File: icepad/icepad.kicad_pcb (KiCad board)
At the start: 2 copper layers, 100 x 100 mm, 56 parts, among them J1 Conn_01x04, J2 USB_B_Mini, U1 STM32F042K6Tx, U2 USBLC6-2SC6, U3 TLV62568DRL

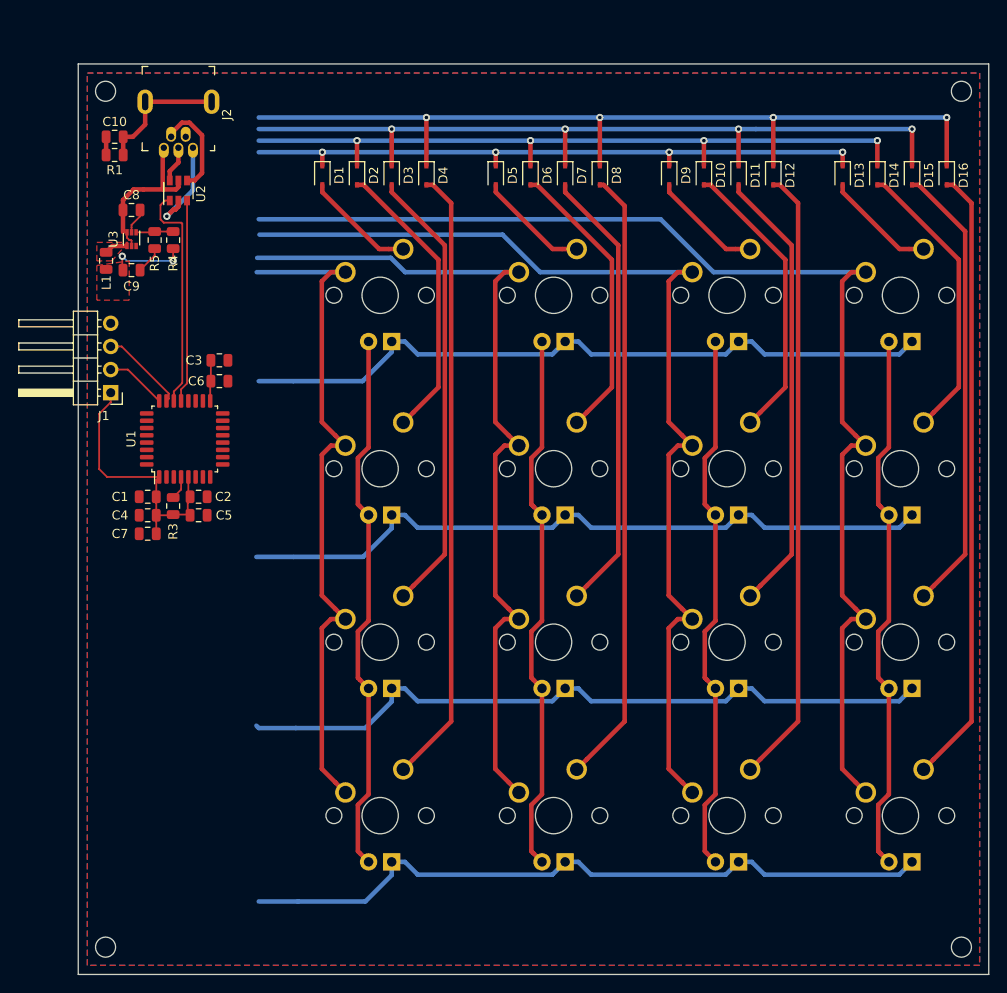
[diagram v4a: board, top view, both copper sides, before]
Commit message: Completed routing, added LED resistors
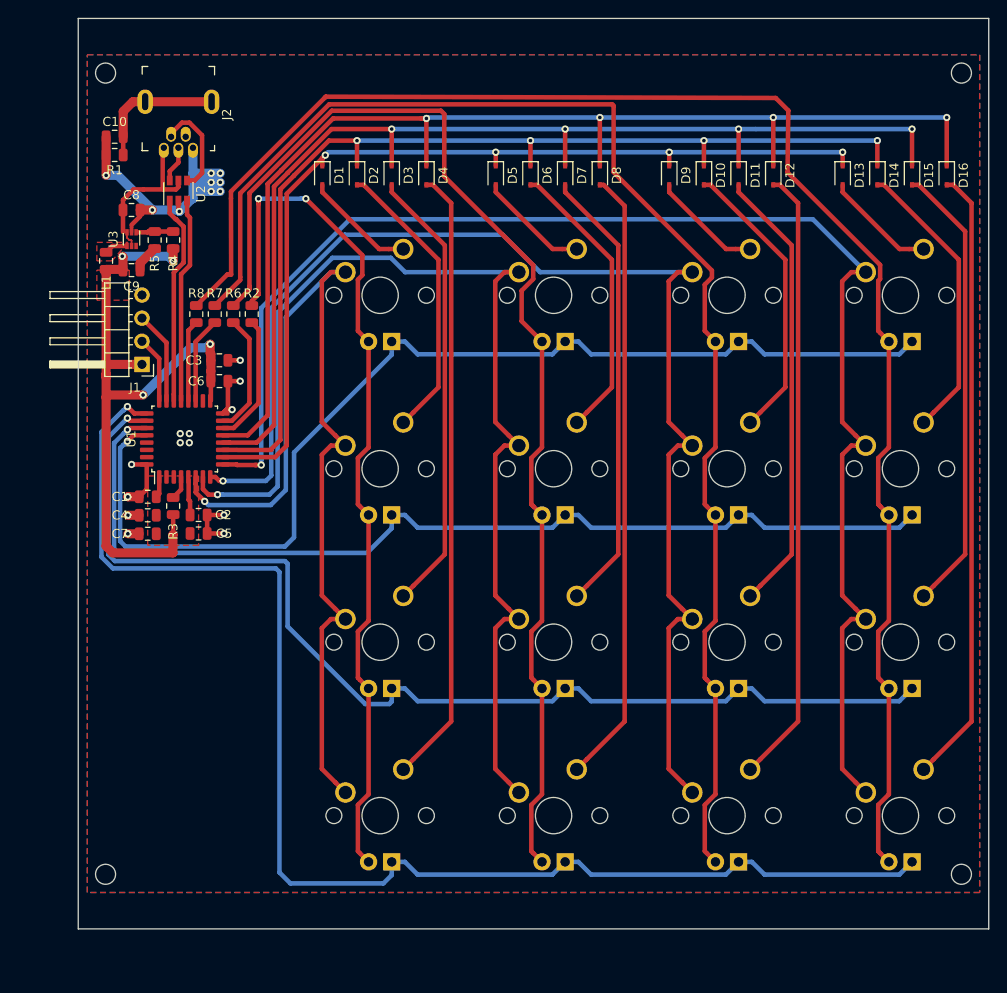
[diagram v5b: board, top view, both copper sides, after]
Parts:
- removed the MNT at (177.0, 147.0)
- removed the MNT at (83.0, 147.0)
- removed the MNT at (177.0, 53.0)
- added MNT: MountingHole_2.2mm_M2, MountingHole:MountingHole_2.2mm_M2, F.Cu at (177.0, 139.0)
- added MNT: MountingHole_2.2mm_M2, MountingHole:MountingHole_2.2mm_M2, F.Cu at (83.0, 139.0)
- added MNT: MountingHole_2.2mm_M2, MountingHole:MountingHole_2.2mm_M2, F.Cu at (177.0, 51.0)
- added R2: 825, Resistor_SMD:R_0805_2012Metric, F.Cu at (99.1, 77.5)
- added R6: 825, Resistor_SMD:R_0805_2012Metric, F.Cu at (97.0, 77.5)
- added R7: 825, Resistor_SMD:R_0805_2012Metric, F.Cu at (95.0, 77.5)
- added R8: 825, Resistor_SMD:R_0805_2012Metric, F.Cu at (93.0, 77.5)
- moved J1 4.63 mm to (87.0, 83.0)
- moved C2 2.00 mm to (93.2, 99.5)
- moved C5 2.00 mm to (93.2, 101.6)
- moved MNT 2.00 mm to (83.0, 51.0)
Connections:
- MX1 pad 3: Col_0_LED -> Net-(MX1-Pad3)
- MX10 pad 3: Col_2_LED -> Net-(MX10-Pad3)
- MX11 pad 3: Col_2_LED -> Net-(MX10-Pad3)
- MX12 pad 3: Col_2_LED -> Net-(MX10-Pad3)
- MX13 pad 3: Col_3_LED -> Net-(MX13-Pad3)
- MX14 pad 3: Col_3_LED -> Net-(MX13-Pad3)
- MX15 pad 3: Col_3_LED -> Net-(MX13-Pad3)
- MX16 pad 3: Col_3_LED -> Net-(MX13-Pad3)
- MX2 pad 3: Col_0_LED -> Net-(MX1-Pad3)
- MX3 pad 3: Col_0_LED -> Net-(MX1-Pad3)
- MX4 pad 3: Col_0_LED -> Net-(MX1-Pad3)
- MX5 pad 3: Col_1_LED -> Net-(MX5-Pad3)
- MX6 pad 3: Col_1_LED -> Net-(MX5-Pad3)
- MX7 pad 3: Col_1_LED -> Net-(MX5-Pad3)
- MX8 pad 3: Col_1_LED -> Net-(MX5-Pad3)
- MX9 pad 3: Col_2_LED -> Net-(MX10-Pad3)
- U1 pad 10: (no net) -> Row_0_Key
- U1 pad 11: (no net) -> Row_1_Key
- U1 pad 12: (no net) -> Row_2_Key
- U1 pad 13: (no net) -> Row_3_Key
- U1 pad 14: (no net) -> Col_0_LED
- U1 pad 15: (no net) -> Col_1_LED
- U1 pad 19: (no net) -> Col_2_LED
- U1 pad 20: (no net) -> Col_3_LED
- U1 pad 25: (no net) -> Row_3_LED
- U1 pad 26: (no net) -> Row_2_LED
- U1 pad 27: (no net) -> Row_1_LED
- U1 pad 28: (no net) -> Row_0_LED
- U1 pad 6: (no net) -> Col_0_Key
- U1 pad 7: (no net) -> Col_1_Key
- U1 pad 8: (no net) -> Col_2_Key
- U1 pad 9: (no net) -> Col_3_Key
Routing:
- net Net-(MX13-Pad3): track 0.00 -> 170.9 mm
- net Net-(MX10-Pad3): track 0.00 -> 149.9 mm
- net Net-(MX5-Pad3): track 0.00 -> 128.9 mm
- net Net-(MX1-Pad3): track 0.00 -> 97.1 mm, vias 0 -> 2
- net Row_3_LED: track 77.9 -> 148.7 mm, vias 0 -> 1
- net GND: track 19.5 -> 80.4 mm, vias 1 -> 22
- net +3V3: track 43.4 -> 95.2 mm, vias 2 -> 4
- net Col_3_LED: track 60.1 -> 8.96 mm
- net Col_2_LED: track 60.1 -> 9.47 mm
- net Col_1_LED: track 60.1 -> 13.3 mm
- net Col_0_LED: track 60.1 -> 14.2 mm
- net Row_2_LED: track 78.3 -> 122.2 mm, vias 0 -> 1
- net Row_0_LED: track 77.7 -> 120.1 mm, vias 0 -> 1
- net Row_1_Key: track 79.0 -> 113.0 mm
- net Row_0_Key: track 70.1 -> 103.9 mm
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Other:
- net class Default: clearance 0.2 -> 0.13
- net class Key Matrix: clearance 0.2 -> 0.13
- net class POWER added: clearance 0.13, trace_width 1, via_dia 0.8, via_drill 0.4
- rule trace_clearance: 0.2 -> 0.13

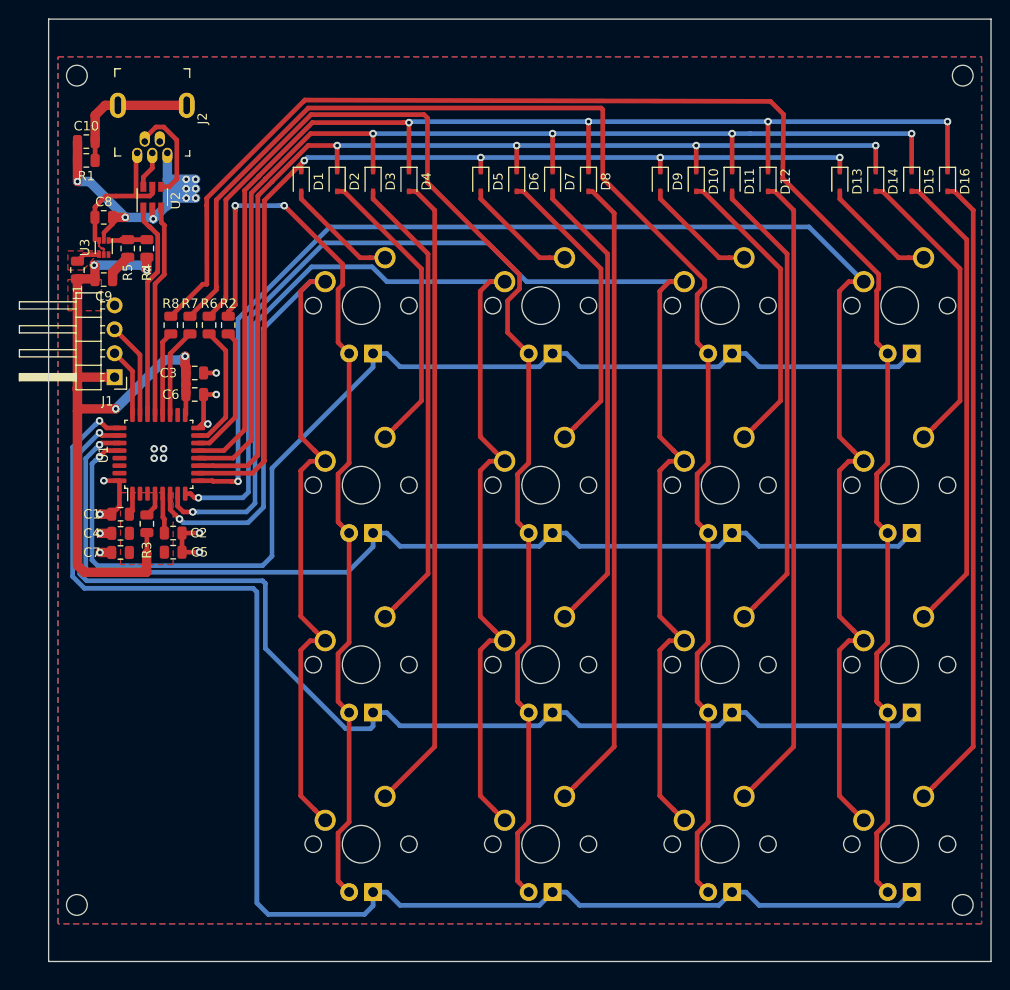
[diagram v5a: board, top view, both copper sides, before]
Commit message: added potentiometers and 3d models
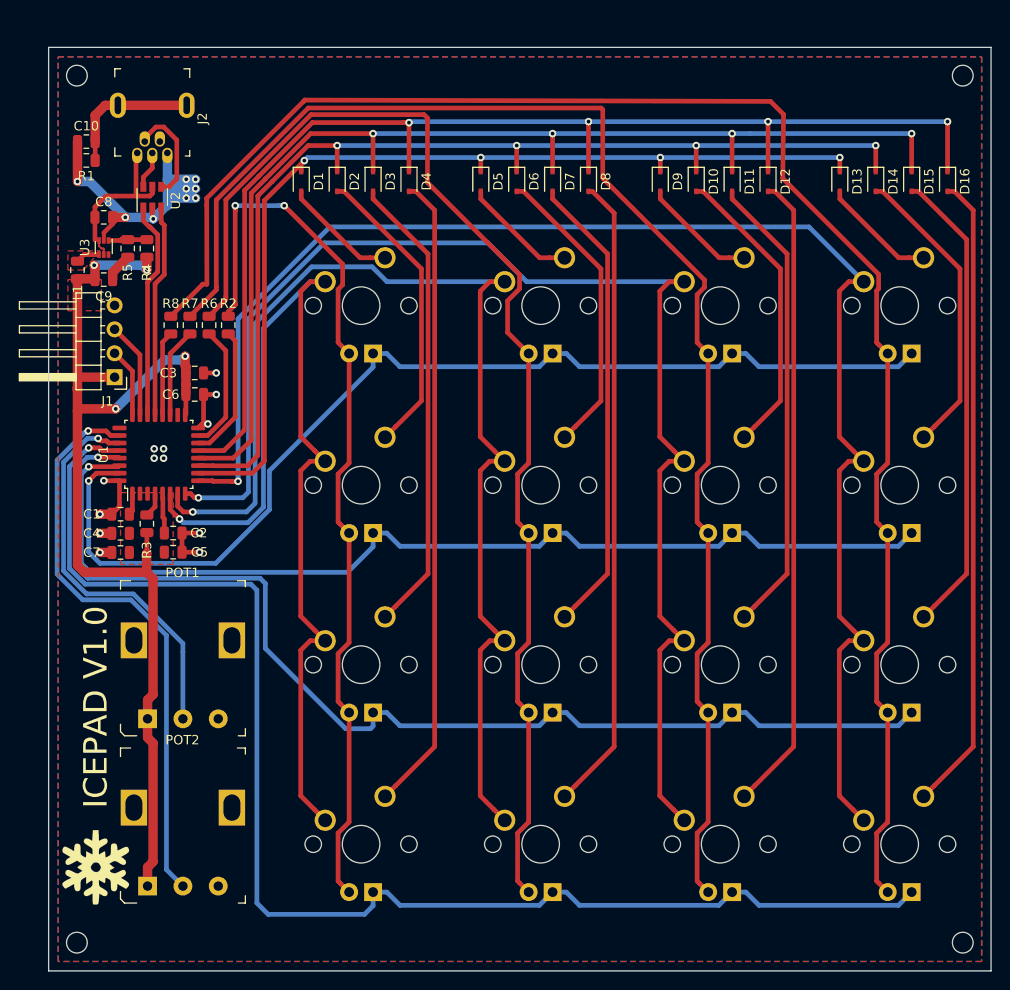
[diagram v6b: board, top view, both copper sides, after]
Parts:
- removed the MNT at (177.0, 139.0)
- removed the MNT at (83.0, 139.0)
- added G***: LOGO, logo:logo, F.Cu at (85.0, 135.0)
- added MNT: MountingHole_2.2mm_M2, MountingHole:MountingHole_2.2mm_M2, F.Cu at (177.0, 143.0)
- added MNT: MountingHole_2.2mm_M2, MountingHole:MountingHole_2.2mm_M2, F.Cu at (83.0, 143.0)
- added POT1: P120PK-Y25BR10K, pot:Potentiometer_P120PK-Y25BR10K, F.Cu at (90.5, 119.2)
- added POT2: P120PK-Y25BR10K, pot:Potentiometer_P120PK-Y25BR10K, F.Cu at (90.5, 137.0)
- J2: footprint digikey-footprints:USB_Mini_B_Female_548190519 -> usb:USB_Mini_B_Female_548190519
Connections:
- U1 pad 25: Row_3_LED -> (no net)
- U1 pad 26: Row_2_LED -> POT2
- U1 pad 27: Row_1_LED -> POT1
- U1 pad 28: Row_0_LED -> Row_3_LED
- U1 pad 29: (no net) -> Row_2_LED
- U1 pad 30: (no net) -> Row_1_LED
- U1 pad 31: (no net) -> Row_0_LED
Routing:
- net POT2: track 0.00 -> 61.8 mm, vias 0 -> 1
- net POT1: track 0.00 -> 42.6 mm, vias 0 -> 1
- net +3V3: track 95.2 -> 129.5 mm
- net Row_0_LED: track 120.1 -> 115.0 mm
- net Row_3_LED: track 148.7 -> 146.3 mm
- net Row_2_LED: track 122.2 -> 120.5 mm
- net Row_1_LED: track 109.8 -> 108.5 mm
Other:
- board size 100 x 100 mm -> 100 x 98 mm
- board text added: "ICEPAD V1.0"

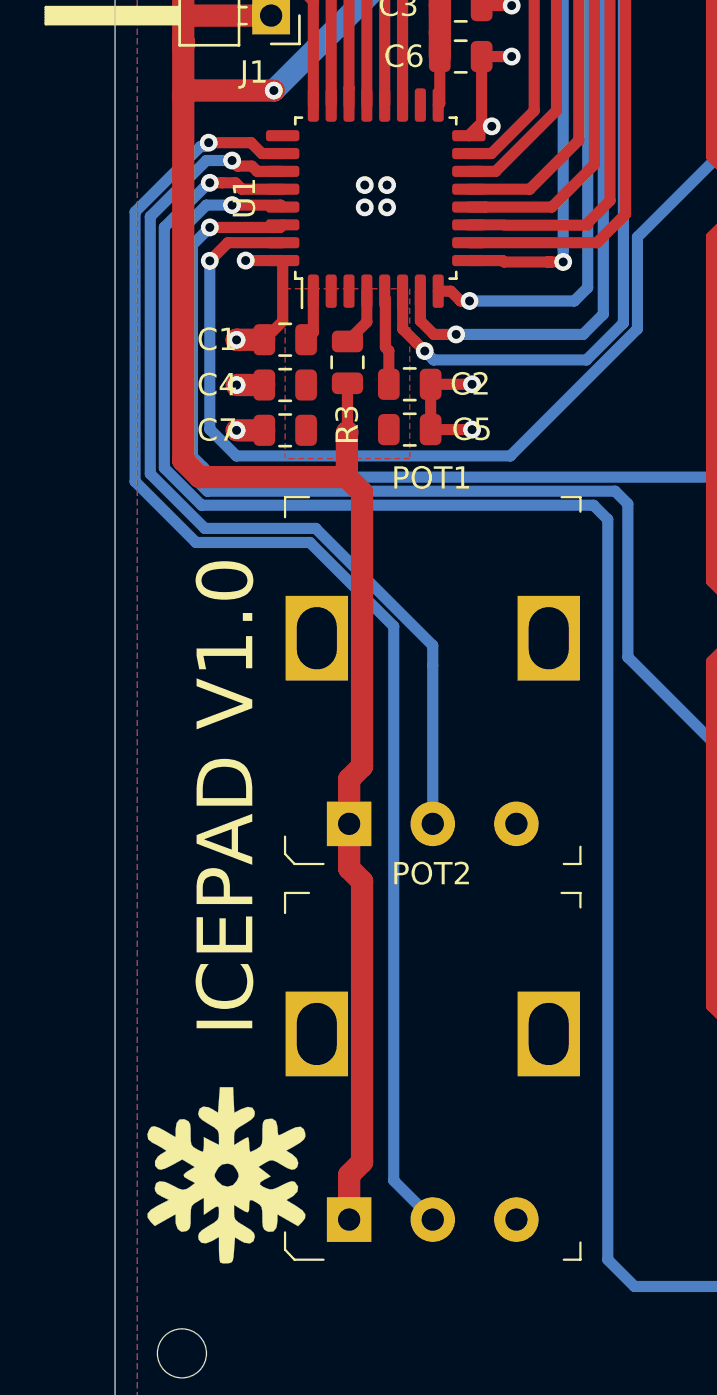
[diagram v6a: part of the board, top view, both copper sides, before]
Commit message: changed potentiometer
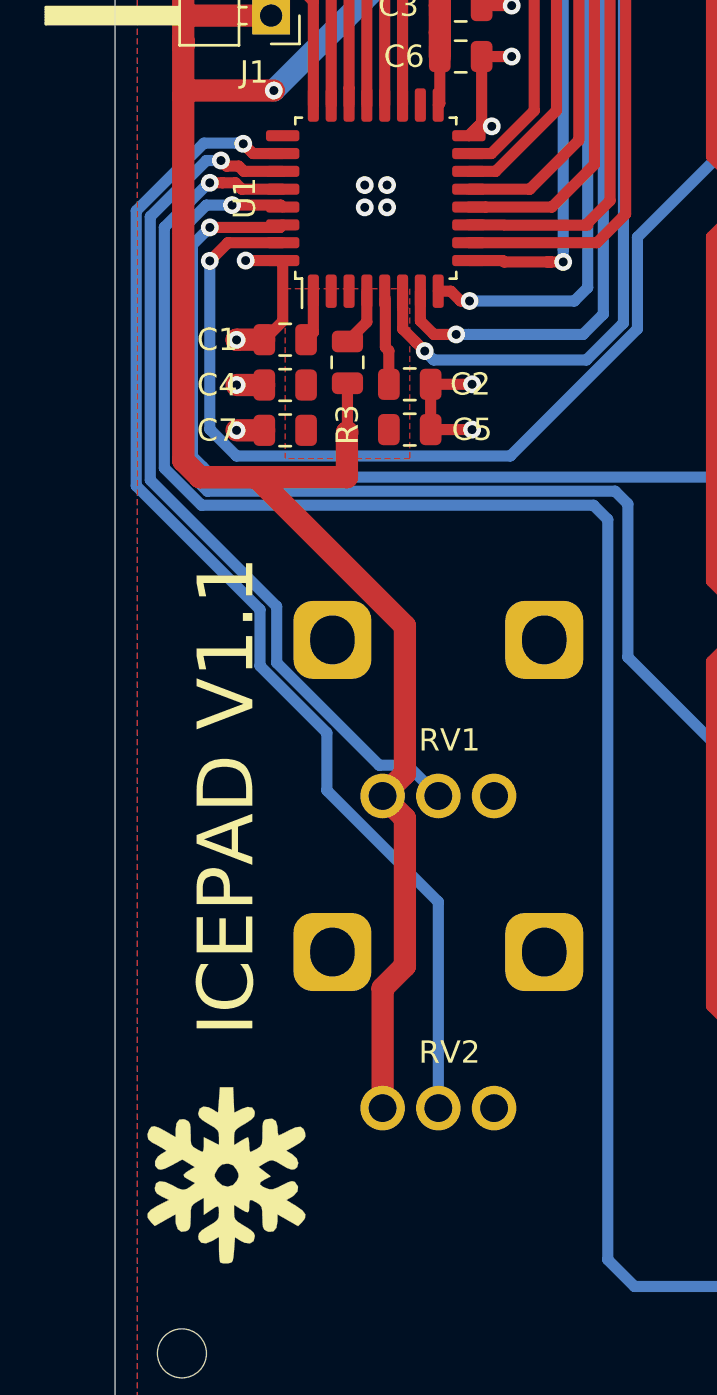
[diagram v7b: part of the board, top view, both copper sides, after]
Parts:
- removed POT1, POT2: P120PK-Y25BR10K, pot:Potentiometer_P120PK-Y25BR10K
- added RV1: R_POT, pot:RK09K1130A5R, F.Cu at (92.0, 118.0)
- added RV2: R_POT, pot:RK09K1130A5R, F.Cu at (92.0, 132.0)
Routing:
- net POT2: track 61.8 -> 53.9 mm
- net POT1: track 42.6 -> 39.3 mm
- net +3V3: track 129.5 -> 130.0 mm
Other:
- board text added: "ICEPAD V1.1"
- board text removed: "ICEPAD V1.0"
